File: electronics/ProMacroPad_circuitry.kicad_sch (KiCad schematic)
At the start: 11 parts, among them J1 Conn_01x06, J2 Conn_01x04, J3 Conn_01x03, P1 Conn_02x20_Odd_Even, U1 quad_level_shifter

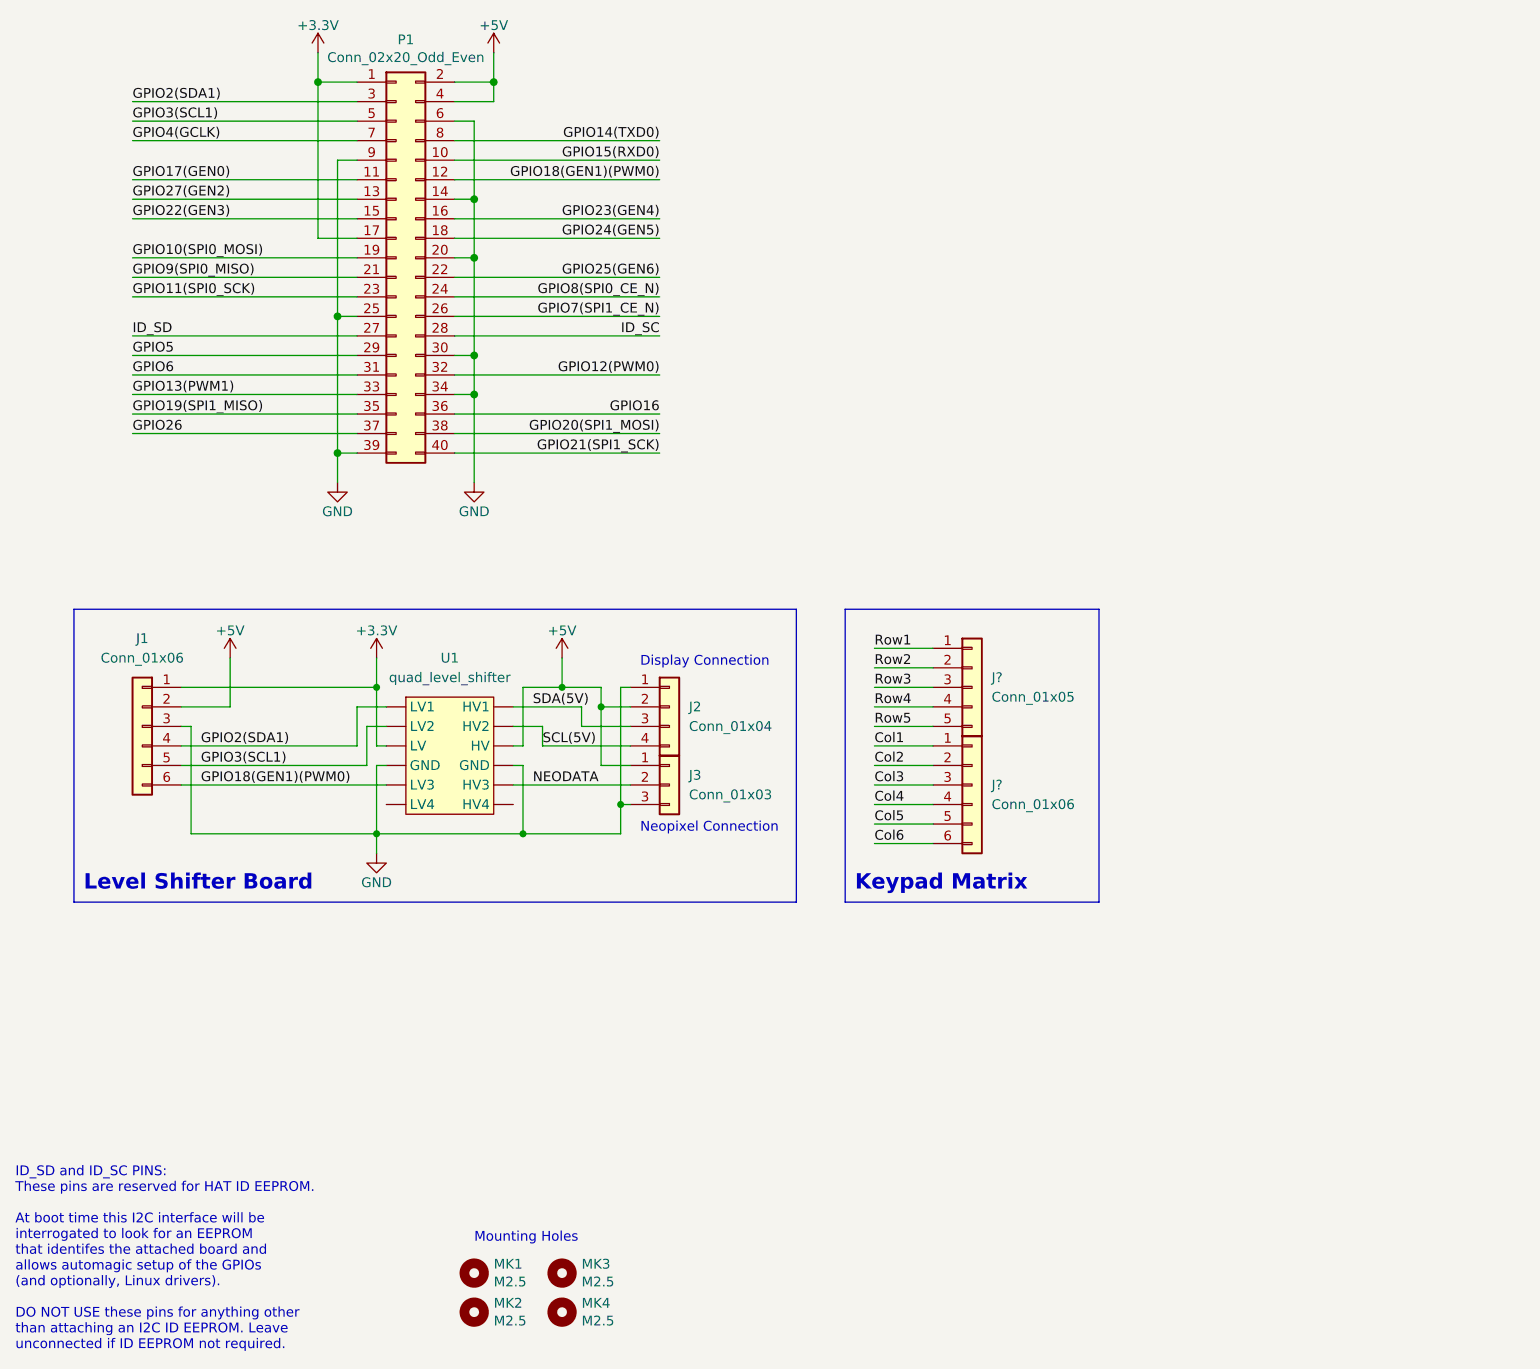
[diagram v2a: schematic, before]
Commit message: updated schematic with the GPIO assignments
these are the GPIO assignments encoded in the device tree source
file, and they are what is currently connected in the prototype.
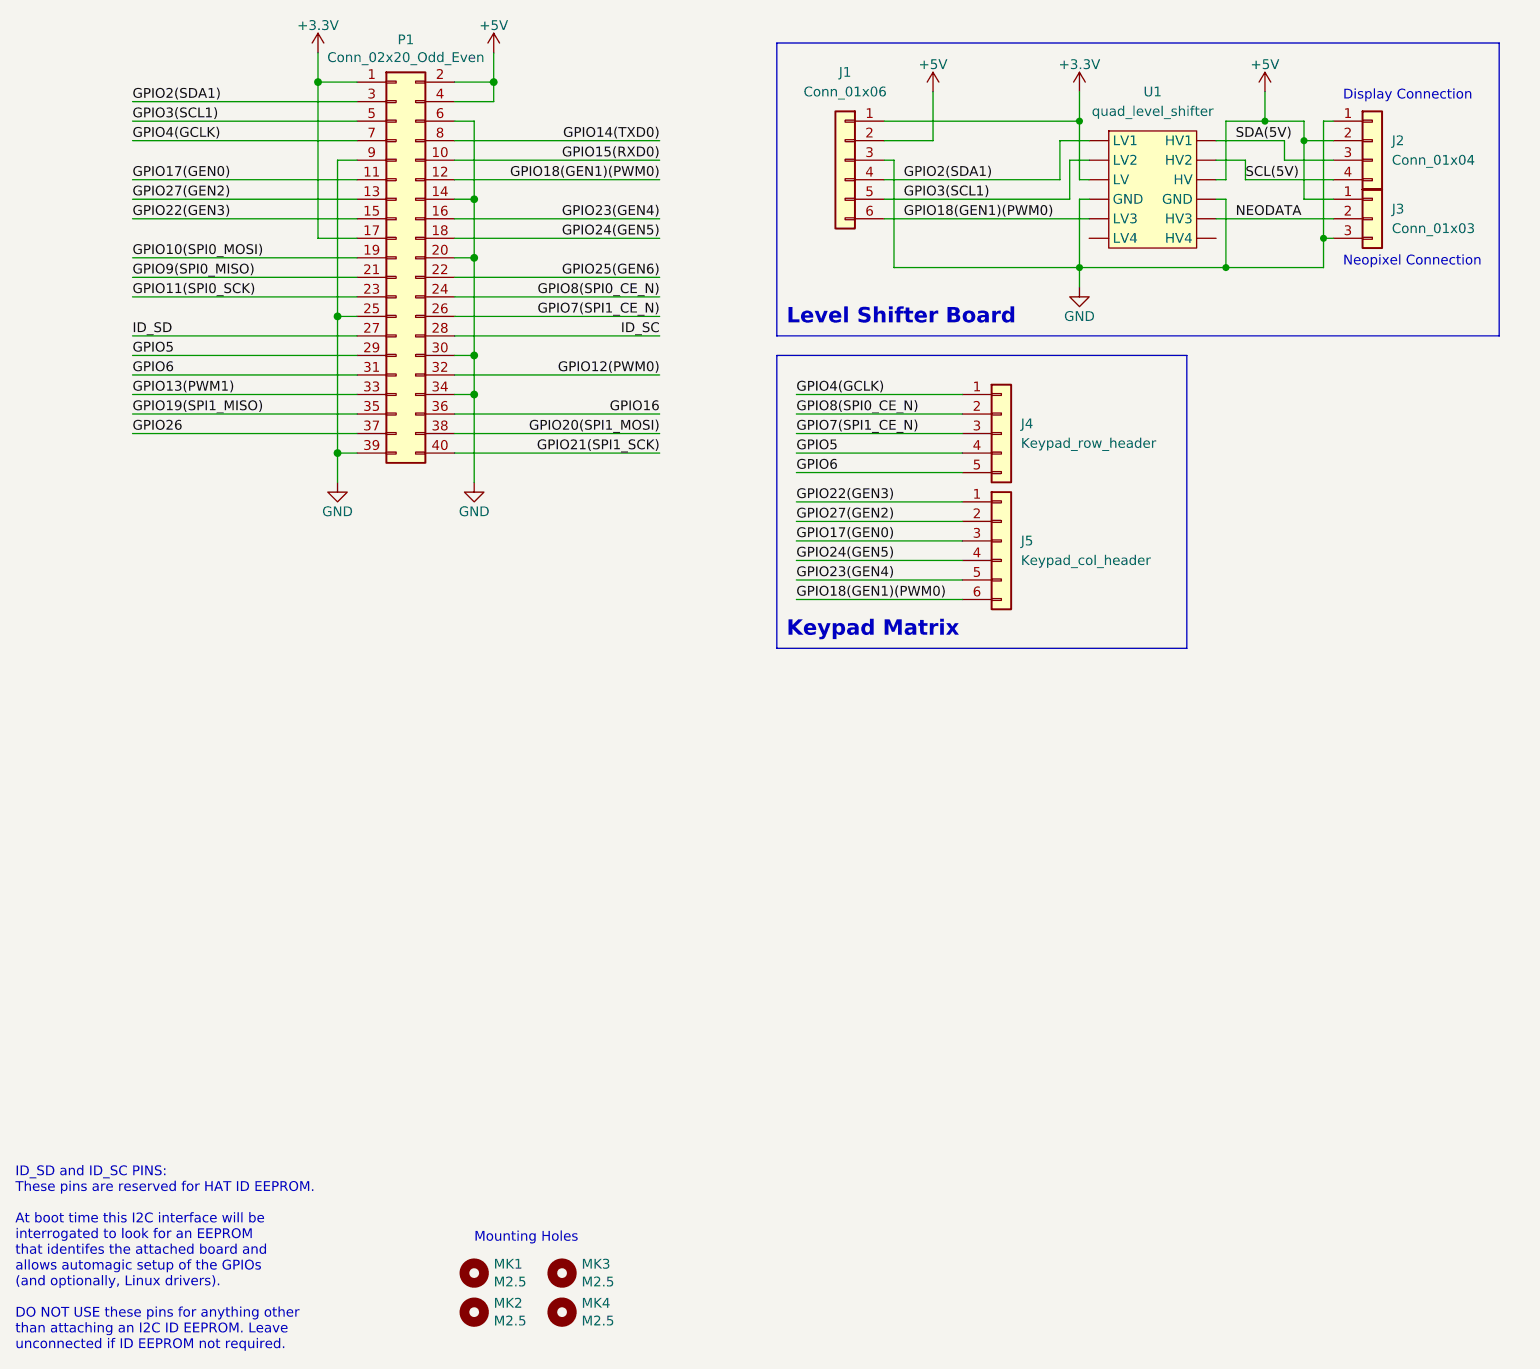
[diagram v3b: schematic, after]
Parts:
- removed J?: Conn_01x06, symbol Connector_Generic:Conn_01x06
- removed J?: Conn_01x05, symbol Connector_Generic:Conn_01x05
- added J4: Keypad_row_header, Connector_PinHeader_2.54mm:PinHeader_1x05_P2.54mm_Horizontal, symbol Connector_Generic:Conn_01x05
- added J5: Keypad_col_header, Connector_PinHeader_2.54mm:PinHeader_1x06_P2.54mm_Horizontal, symbol Connector_Generic:Conn_01x06
- P1: now in the parts list
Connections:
- net GPIO17(GEN0): now also J5.3 (Pin_3)
- net GPIO18(GEN1)(PWM0): now also J5.6 (Pin_6)
- net GPIO22(GEN3): now also J5.1 (Pin_1)
- net GPIO23(GEN4): now also J5.5 (Pin_5)
- net GPIO24(GEN5): now also J5.4 (Pin_4)
- net GPIO27(GEN2): now also J5.2 (Pin_2)
- net GPIO4(GCLK): now also J4.1 (Pin_1)
- net GPIO5: now also J4.4 (Pin_4)
- net GPIO6: now also J4.5 (Pin_5)
- net GPIO7(SPI1_CE_N): now also J4.3 (Pin_3)
- net GPIO8(SPI0_CE_N): now also J4.2 (Pin_2)
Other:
- moved on the sheet: J1, J2, J3, U1
